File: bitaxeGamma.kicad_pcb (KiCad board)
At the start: 4 copper layers, 56.5 x 99.8 mm, 131 parts, among them J1 54-00164, J2 TC2030-IDC, J3 Conn_01x04, J4 Conn_01x06, J5 USB_C_Receptacle_USB2.0, J6 Conn_01x04, J7 Conn_01x04, SW1 GT-TC029B-H025-L1N, SW2 GT-TC029B-H025-L1N, T1 net-tie, U10 EMC2101, U2 TPS546D24ARVFR, U3 RT9080-33GJ5, U4 ESP32-S3-WROOM-1, U5 MCP1824T-1202E/OT, U6 MCP1824T-0802E, U7 25MHz, U8 BM1370_mode1, U9 SN74AVC4T774

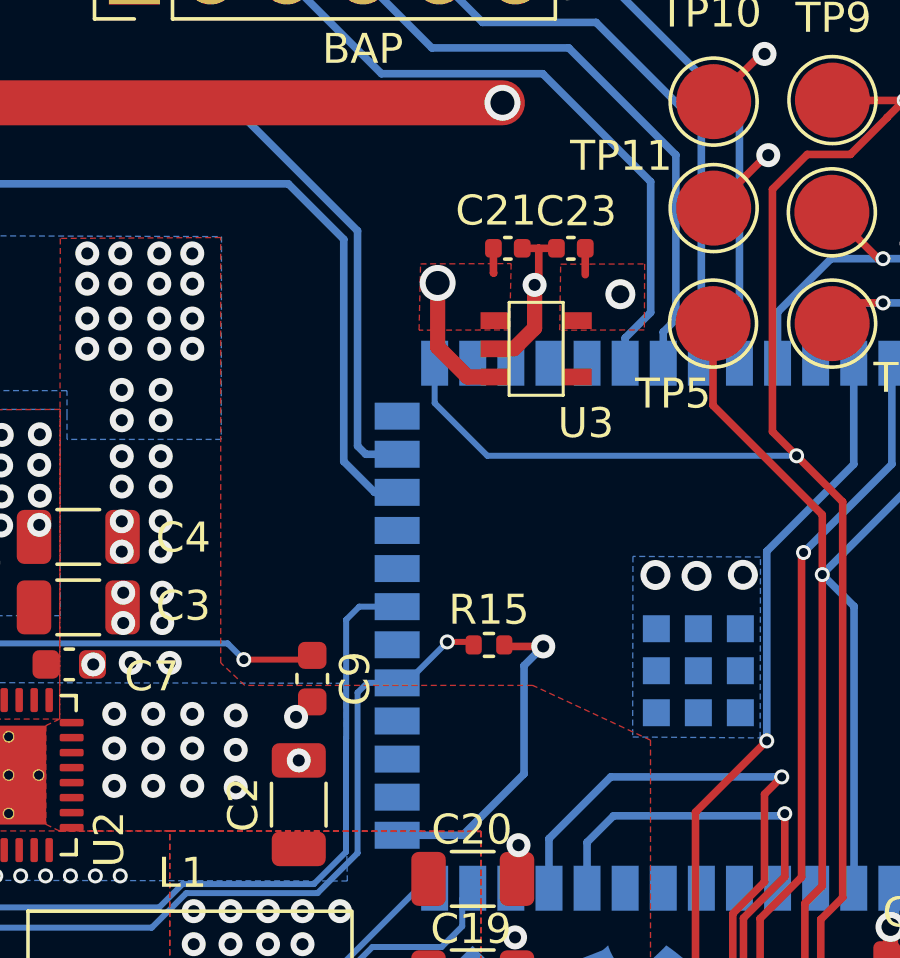
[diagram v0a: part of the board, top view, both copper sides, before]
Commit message: added pullup resistors for #25
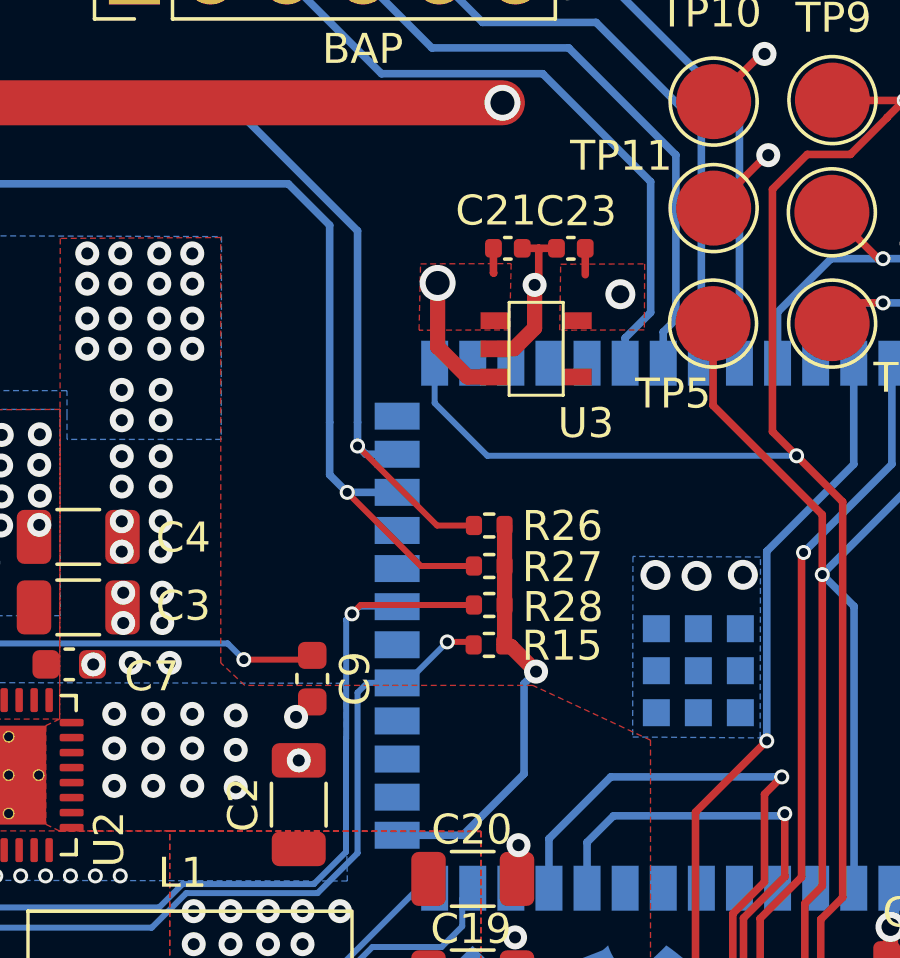
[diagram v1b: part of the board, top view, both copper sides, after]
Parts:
- added R26: 5.6k, Resistor_SMD:R_0402_1005Metric, F.Cu at (111.0, 69.3)
- added R27: 5.6k, Resistor_SMD:R_0402_1005Metric, F.Cu at (111.0, 70.6)
- added R28: 5.6k, Resistor_SMD:R_0402_1005Metric, F.Cu at (111.0, 71.9)
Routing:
- net /SDA: track 137.3 -> 143.1 mm, vias 4 -> 5
- net /SCL: track 140.1 -> 145.0 mm, vias 2 -> 3
- net /Power/PMB_ALRT: track 24.9 -> 29.1 mm, vias 1 -> 2
- net /3V3: track 53.0 -> 56.2 mm

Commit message: Revert "added pullup resistors for #25"
This reverts commit 91572af801fdd590416a5d3df79444bb16faa4cf.
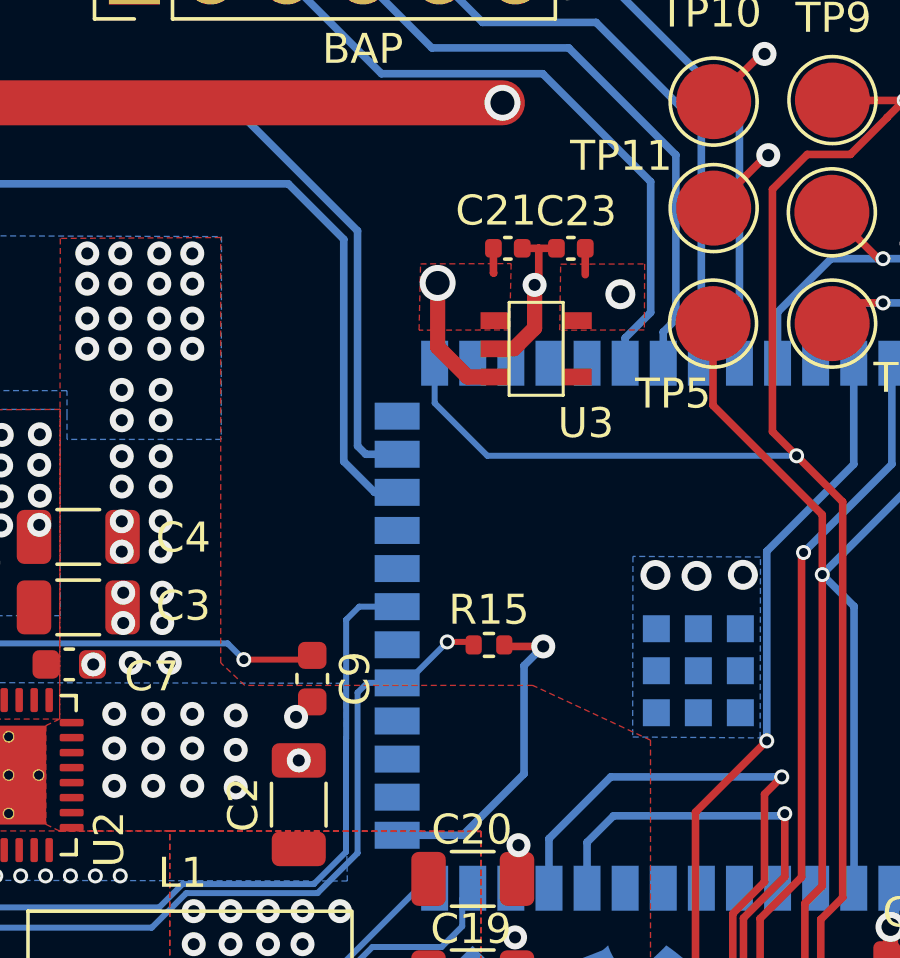
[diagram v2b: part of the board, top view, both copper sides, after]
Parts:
- removed R26, R27, R28: 5.6k, Resistor_SMD:R_0402_1005Metric
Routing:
- net /SDA: track 143.1 -> 137.3 mm, vias 5 -> 4
- net /SCL: track 145.0 -> 140.1 mm, vias 3 -> 2
- net /Power/PMB_ALRT: track 29.1 -> 24.9 mm, vias 2 -> 1
- net /3V3: track 56.2 -> 53.0 mm
